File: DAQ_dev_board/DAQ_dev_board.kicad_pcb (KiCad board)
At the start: 2 copper layers, 82 x 42 mm, 38 parts, among them J1 Thermocouple, J2 Conn_01x16_Pin, J3 Conn_01x08_Pin, J5 Conn_01x08_Pin, U1 ADS1158IRTCR (ADC), U2 AD8495 (TC AMP), U3 OP777ARZ (OP AMP), Y1 32.768kHz

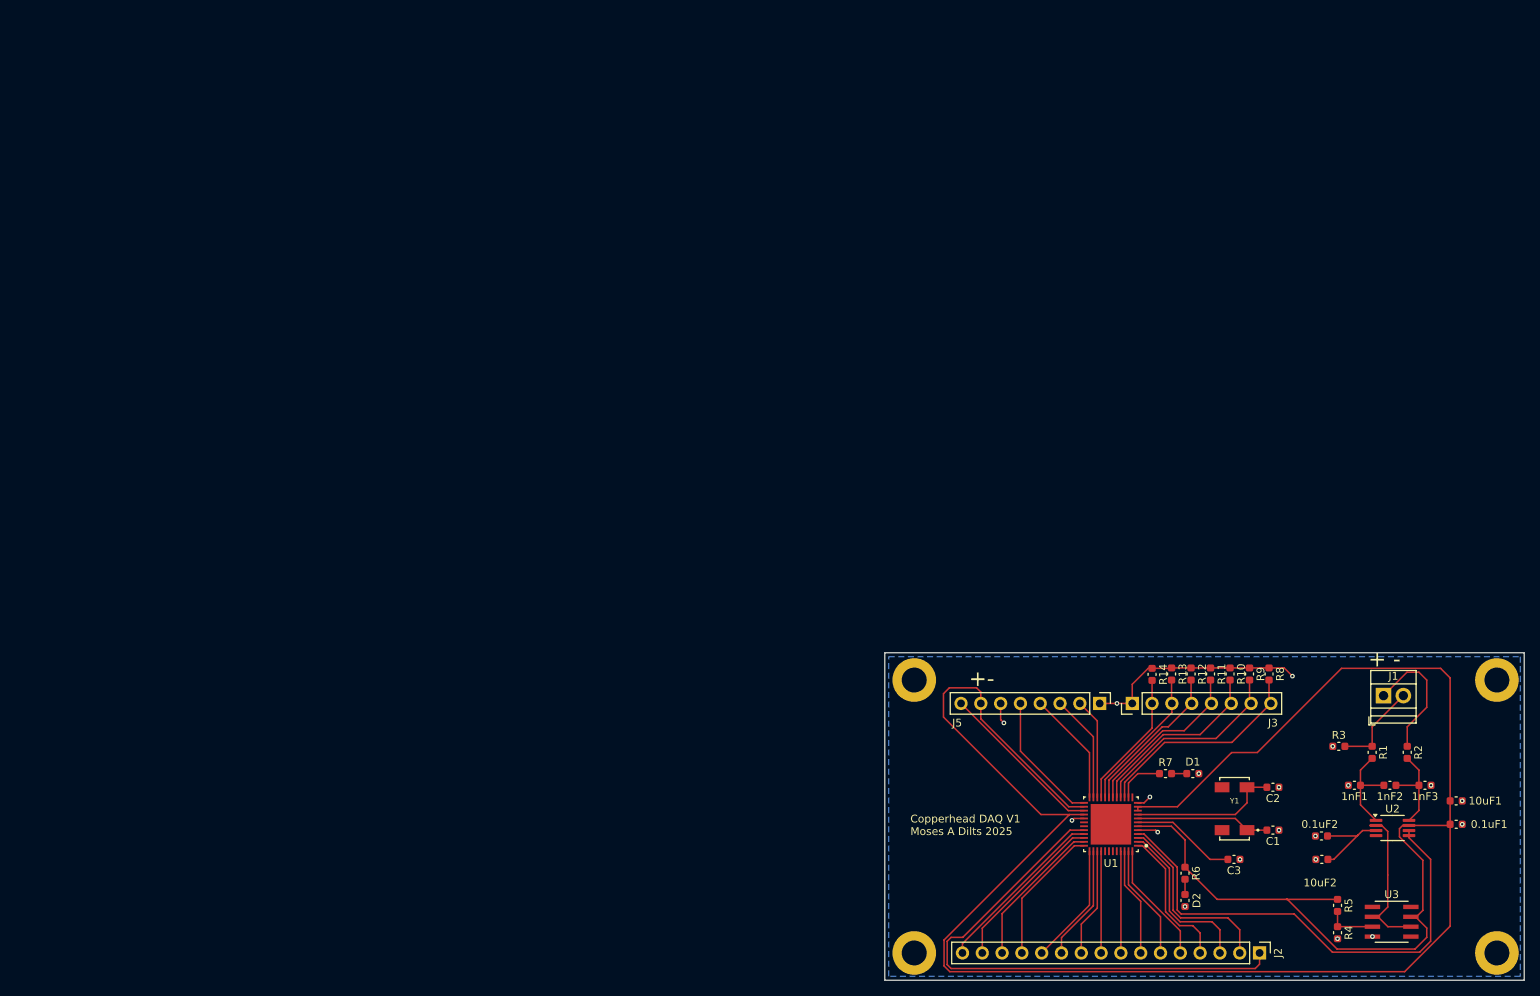
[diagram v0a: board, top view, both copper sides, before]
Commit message: updated DAQ silkscreen to be less dumb
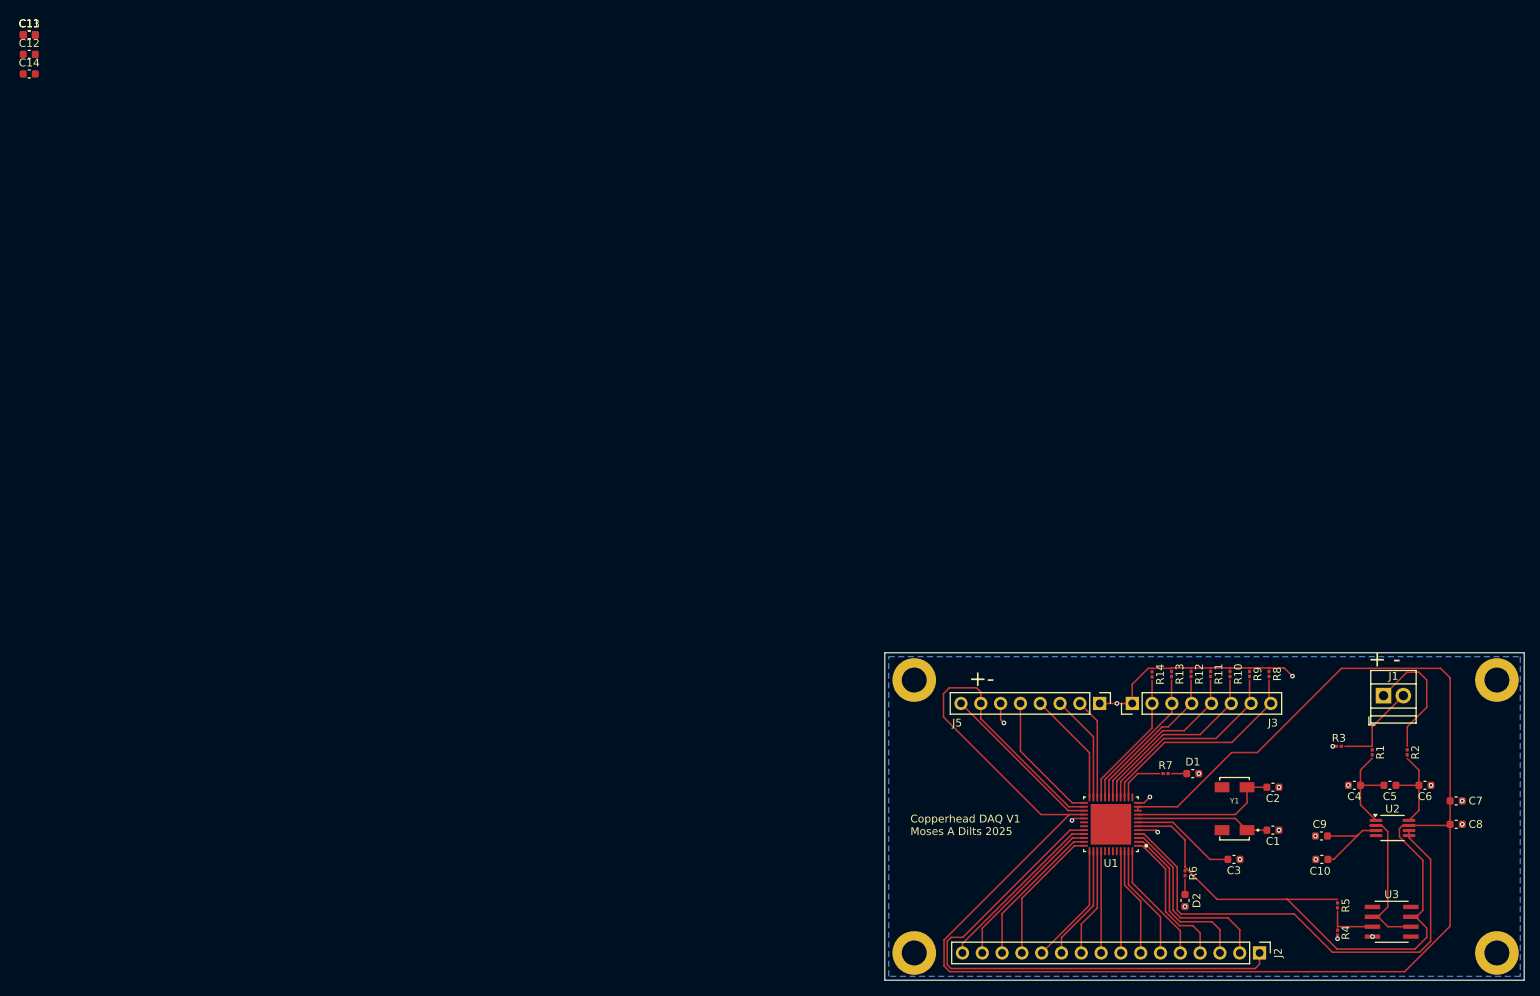
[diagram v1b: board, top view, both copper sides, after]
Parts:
- added C11: 0.1uF, Capacitor_SMD:C_0603_1608Metric, F.Cu at (1.50, 0.76)
- added C12: 10uF, Capacitor_SMD:C_0603_1608Metric, F.Cu at (1.50, 3.27)
- added C13: 10uF, Capacitor_SMD:C_0603_1608Metric, F.Cu at (1.50, 0.76)
- added C14: 0.1uF, Capacitor_SMD:C_0603_1608Metric, F.Cu at (1.50, 5.78)
- C10: renamed from 10uF2; value C7 -> 10uF2
- C4: renamed from 1nF1; value C3 -> 1nF
- C5: renamed from 1nF2; value C2 -> 1nF
- C6: renamed from 1nF3; value C1 -> 1nF
- C7: renamed from 10uF1; value C4 -> 10uF1
- C8: renamed from 0.1uF1; value C5 -> 0.1uF1
- C9: renamed from 0.1uF2; value C6 -> 0.1uF2
- R1, R10, R11, R12, R13, R14, R2, R3, R4, R5, R6, R7, R8, R9: footprint Capacitor_SMD:C_0603_1608Metric -> Resistor_SMD:R_0201_0603Metric
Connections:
- J2 pad 1: Net-(J2-Pin_1) -> GND
- U1 pad 1: Net-(J2-Pin_4) -> Net-(J2-Pin_14)
- U1 pad 2: Net-(J2-Pin_3) -> Net-(J2-Pin_15)
- U1 pad 3: Net-(J2-Pin_2) -> Net-(J2-Pin_16)
- U1 pad 30: unconnected-(U1-VREFN-Pad30) -> GND
- U1 pad 31: unconnected-(U1-VREFP-Pad31) -> +5V
- U1 pad 32: Net-(J2-Pin_1) -> GND
- U1 pad 33: Net-(J2-Pin_16) -> Net-(J2-Pin_2)
- U1 pad 34: Net-(J2-Pin_15) -> Net-(J2-Pin_3)
- U1 pad 35: Net-(J2-Pin_14) -> Net-(J2-Pin_4)
- U1 pad 36: Net-(J2-Pin_13) -> Net-(J2-Pin_5)
- U1 pad 37: Net-(J2-Pin_12) -> Net-(J2-Pin_6)
- U1 pad 38: Net-(J2-Pin_11) -> Net-(J2-Pin_7)
- U1 pad 39: Net-(J2-Pin_10) -> Net-(J2-Pin_8)
- U1 pad 45: Net-(J2-Pin_8) -> Net-(J2-Pin_10)
- U1 pad 46: Net-(J2-Pin_7) -> Net-(J2-Pin_11)
- U1 pad 47: Net-(J2-Pin_6) -> Net-(J2-Pin_12)
- U1 pad 48: Net-(J2-Pin_5) -> Net-(J2-Pin_13)
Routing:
- net Net-(J2-Pin_1): track 68.4 -> 0.00 mm
- net GND: track 49.3 -> 117.7 mm

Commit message: sync
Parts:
- C10: value 10uF2 -> 10uF
- C7: value 10uF1 -> 10uF
- C8: value 0.1uF1 -> 0.1uF
- C9: value 0.1uF2 -> 0.1uF
- R1, R10, R11, R12, R13, R14, R2, R3, R4, R5, R6, R7, R8, R9: footprint Resistor_SMD:R_0201_0603Metric -> Resistor_SMD:R_0603_1608Metric
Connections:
- C7 pad 1: GND -> +5V
- C7 pad 2: +5V -> GND
- C8 pad 1: GND -> +5V
- C8 pad 2: +5V -> GND
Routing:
- net GND: vias 20 -> 18
- net +5V: vias 0 -> 2
